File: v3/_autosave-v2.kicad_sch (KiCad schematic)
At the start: 112 parts, among them J2 Conn_01x04_Pin, J3 Conn_01x04_Pin, SW1 SW_Push, SW10 SW_Push, SW11 SW_Push, SW12 SW_Push, SW13 SW_Push, SW14 SW_Push, SW15 SW_Push, SW16 SW_Push, SW17 SW_Push, SW18 SW_Push, SW19 SW_Push, SW2 SW_Push, SW20 SW_Push, SW21 SW_Push, SW22 SW_Push, SW23 SW_Push, SW24 SW_Push, SW25 SW_Push, SW26 SW_Push, SW27 SW_Push, SW28 SW_Push, SW29 SW_Push, SW3 SW_Push, SW30 SW_Push, SW31 SW_Push, SW32 SW_Push, SW33 RotaryEncoder_Switch, SW4 SW_Push, SW5 SW_Push, SW6 SW_Push, SW7 SW_Push, SW8 SW_Push, SW9 SW_Push, U1 Pico, U2 Pico

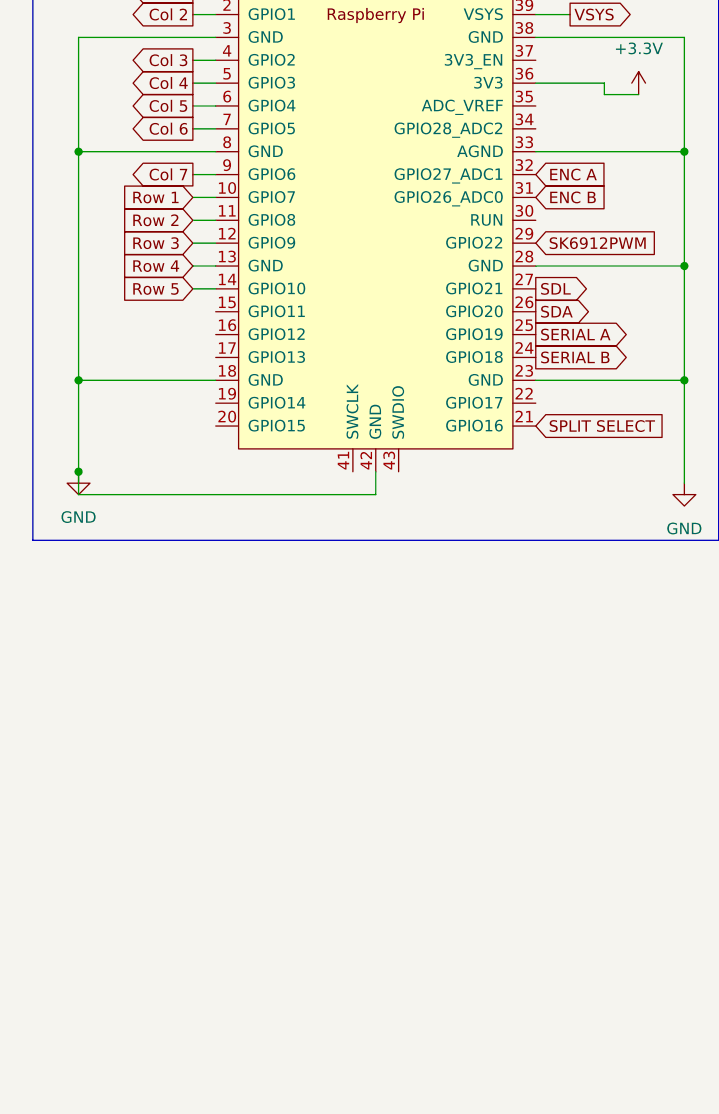
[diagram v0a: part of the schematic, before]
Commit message: started adding the nice!nano footprints
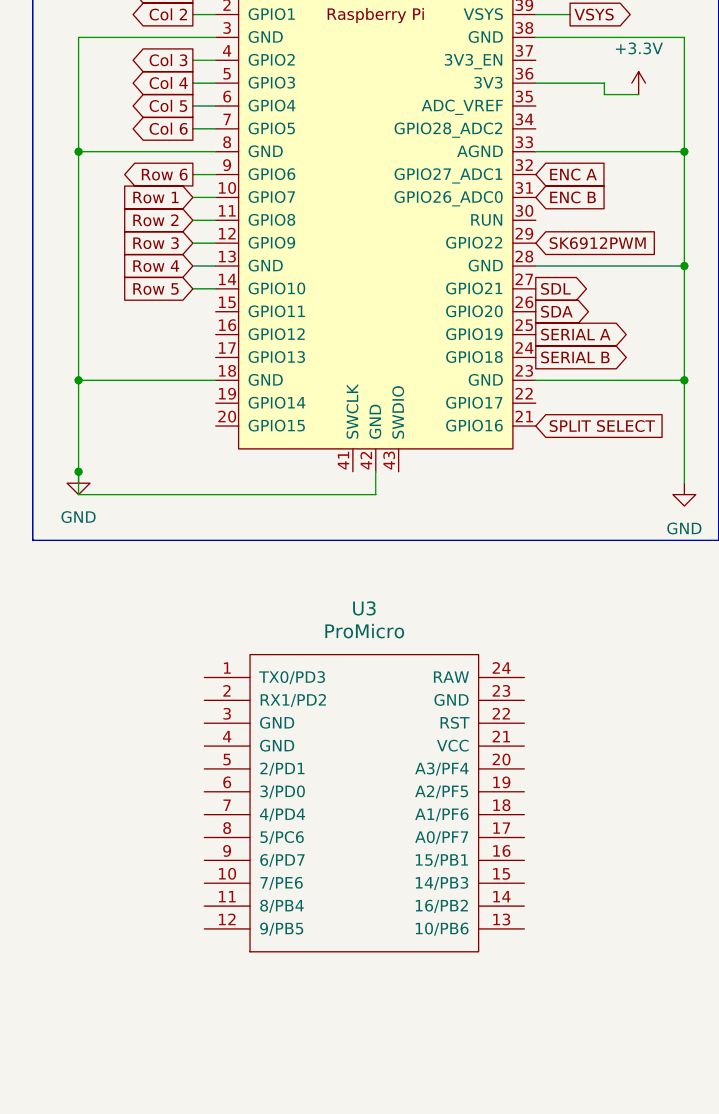
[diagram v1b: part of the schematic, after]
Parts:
- added U3: ProMicro, symbol keebio:ProMicro
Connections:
- net Col 7: no longer U2.9 (GPIO6)
- net Row 6: now also U2.9 (GPIO6)
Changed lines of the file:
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@@
 		)
 	)
-	(global_label "Col 7"
+	(global_label "Row 6"
 		(shape output)
 		(at 41.91 147.32 180)
@@
 		)
 		(property "Intersheetrefs" "${INTERSHEET_REFS}"
-			(at 33.6635 147.32 0)
+			(at 32.9982 147.32 0)
 			(effects
 				(font
@@
 					(unit 1)
 				)
+			)
+		)
+	)
+	(symbol
+		(lib_id "keebio:ProMicro")
+		(at 60.96 217.17 0)
+		(unit 1)
+		(exclude_from_sim no)
+		(in_bom yes)
+		(on_board yes)
+		(dnp no)
+		(fields_autoplaced yes)
+		(property "Reference" "U3"
+			(at 60.96 195.58 0)
+			(effects
+				(font
+					(size 1.524 1.524)
+				)
+			)
+		)
+		(property "Value" "ProMicro"
+			(at 60.96 198.12 0)
+			(effects
+				(font
+					(size 1.524 1.524)
+				)
+			)
+		)
+		(property "Footprint" ""
+			(at 87.63 280.67 90)
+			(effects
+				(font
+					(size 1.524 1.524)
+				)
+				(hide yes)
+			)
+		)
+		(property "Datasheet" ""
+			(at 87.63 280.67 90)
+			(effects
+				(font
+					(size 1.524 1.524)
+				)
+				(hide yes)
+			)
+		)
+		(property "Description" ""
+			(at 60.96 217.17 0)
+			(effects
+				(font
+					(size 1.27 1.27)
+				)
+				(hide yes)
+			)
+		)
+		(pin "17"
+		)
+		(pin "24"
+		)
+		(pin "11"
+		)
+		(pin "15"
+		)
+		(pin "10"
+		)
+		(pin "2"
+		)
+		(pin "14"
+		)
+		(pin "20"
+		)
+		(pin "21"
+		)
+		(pin "12"
+		)
+		(pin "13"
+		)
+		(pin "18"
+		)
+		(pin "6"
+		)
+		(pin "7"
+		)
+		(pin "1"
+		)
+		(pin "19"
+		)
+		(pin "3"
+		)
+		(pin "5"
+		)
+		(pin "8"
+		)
+		(pin "9"
+		)
+		(pin "23"
+		)
+		(pin "4"
+		)
+		(pin "22"
+		)
+		(pin "16"
+		)
+		(instances
+			(project ""
+				(path "/83915211-7eef-4799-b632-bb05dde16da3"
+					(reference "U3")
+					(unit 1)
+				)
